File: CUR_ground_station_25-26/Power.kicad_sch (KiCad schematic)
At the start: 27 parts, among them J1 Conn_01x02, J2 UJ20-C-H-G-SMT-P16-TR, Q2 NTR4003N, SW5 PTS815SJM250SMTRLFS, U2 BQ24232RGT, U3 NCP186AMX330TAG, U4 USBLC6-2SC6

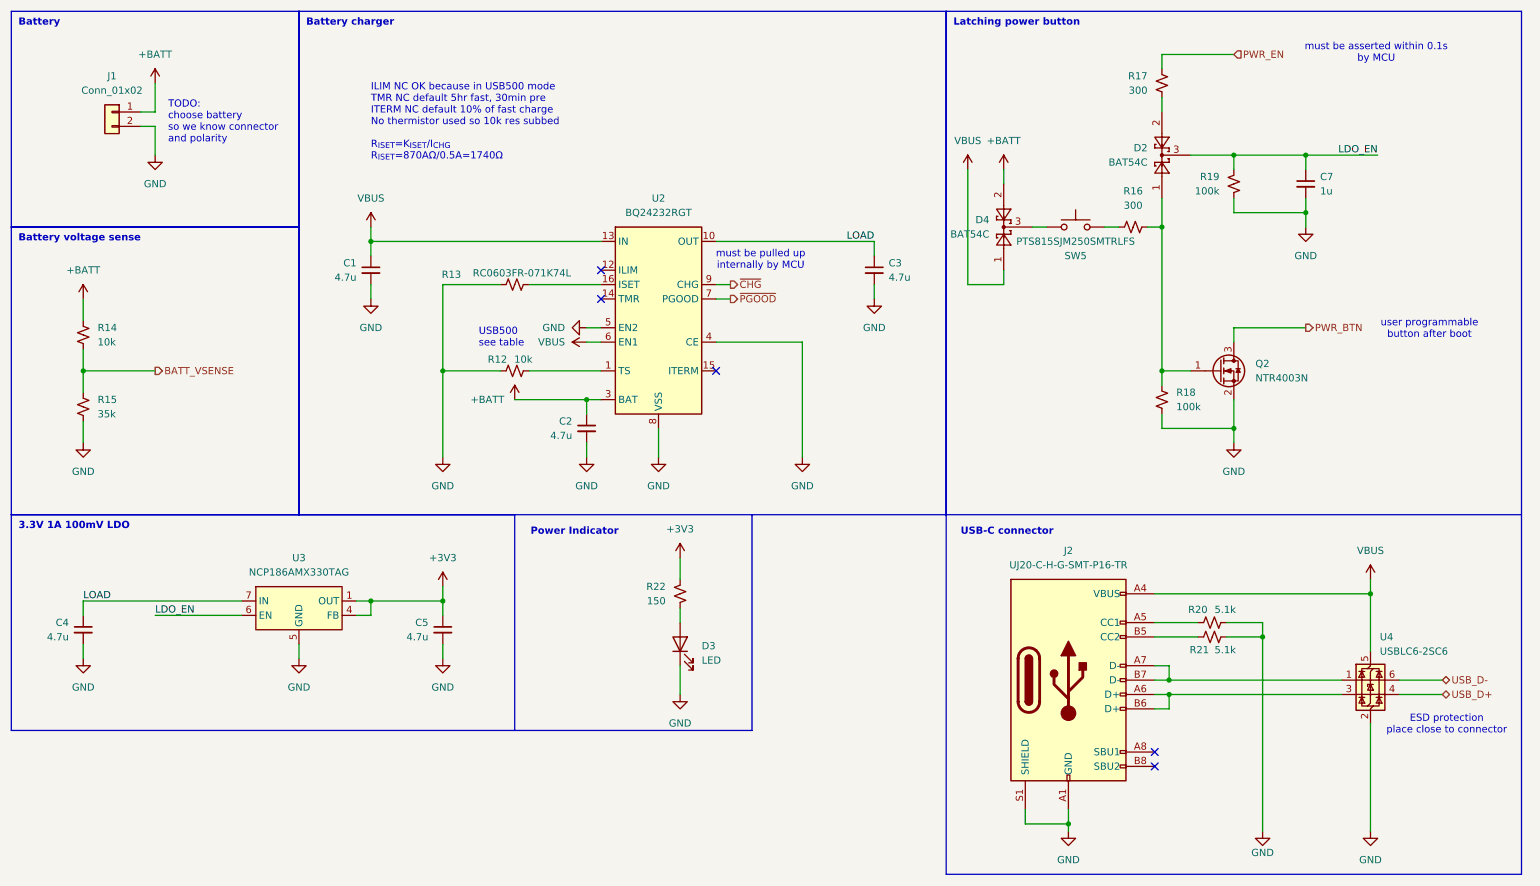
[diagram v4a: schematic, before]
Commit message: Add testpoints to power
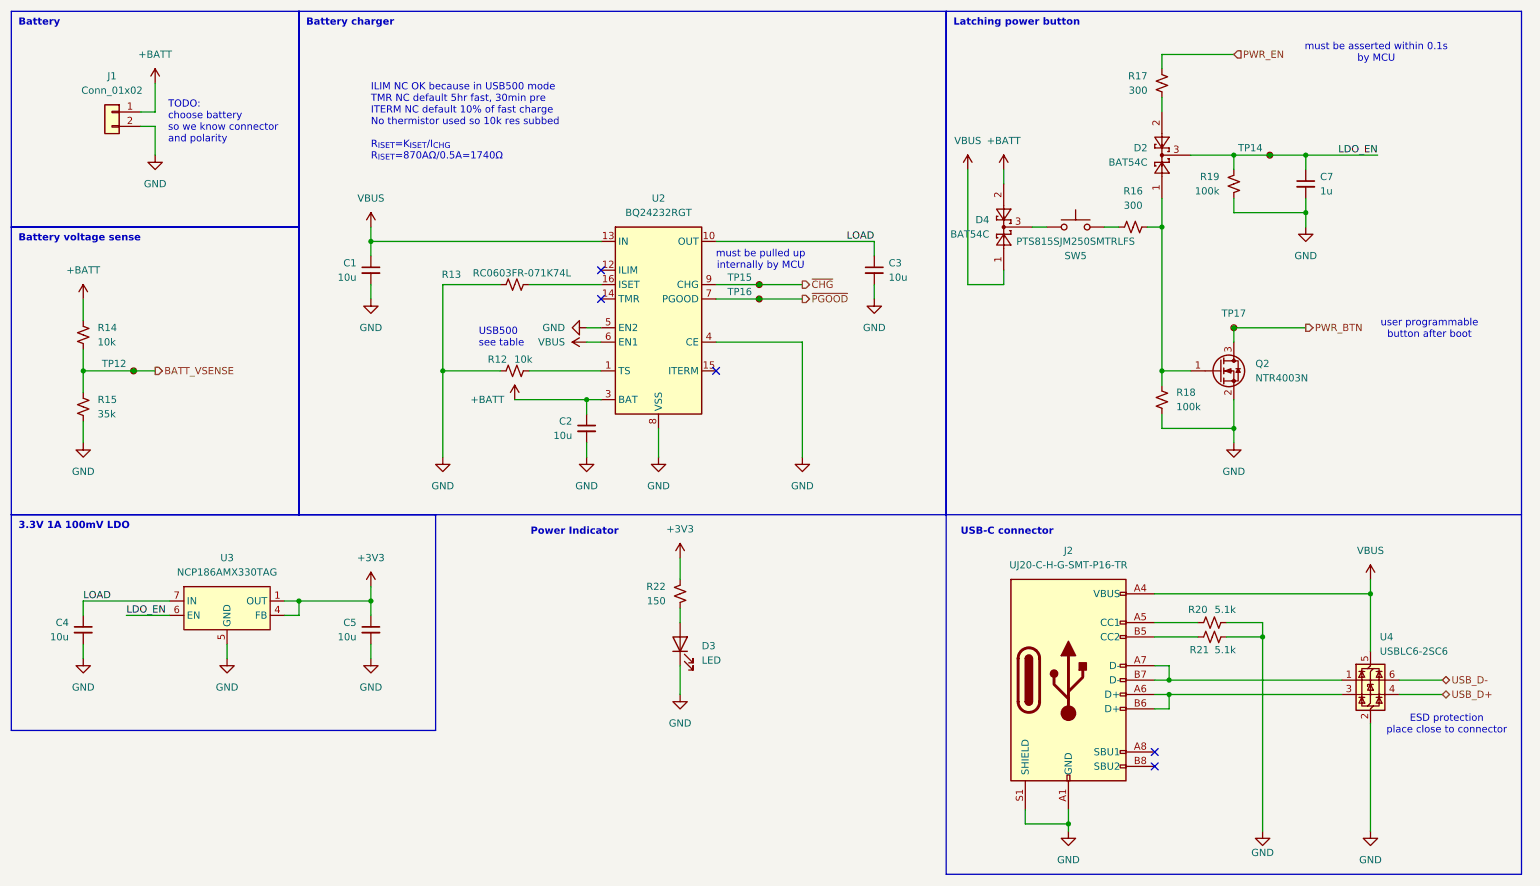
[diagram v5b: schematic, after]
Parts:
- added TP12, TP14, TP15, TP16, TP17: TestPoint_Small, TestPoint_KOASpeer:TestPoint_Chip_RCUCTE_0603, symbol Connector:TestPoint_Small
- C1, C2, C3, C4, C5: value 4.7u -> 10u
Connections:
- net BATT_VSENSE: now also TP12.1
- net LDO_EN: now also TP14.1
- net PWR_BTN: now also TP17.1
- net ~{CHG}: now also TP15.1
- net ~{PGOOD}: now also TP16.1
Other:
- moved on the sheet: C5, U3

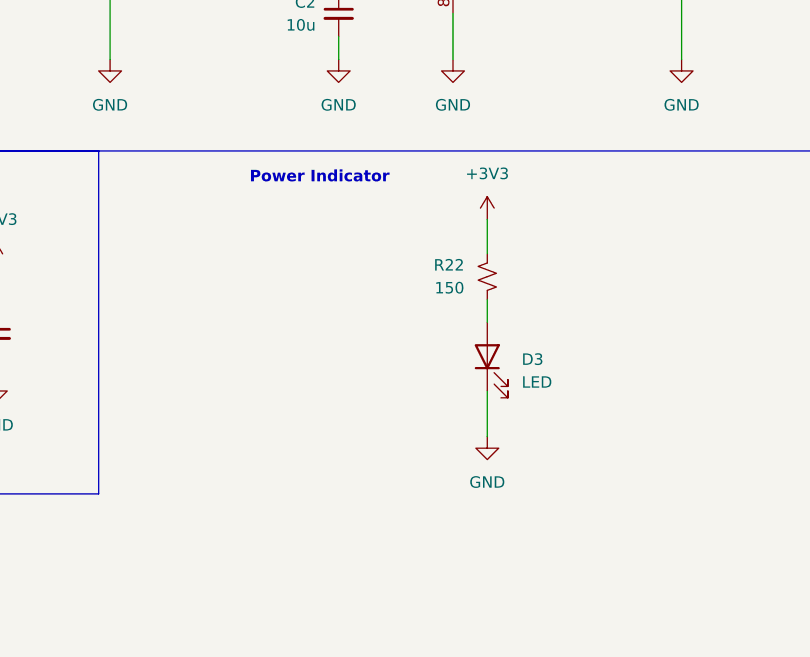
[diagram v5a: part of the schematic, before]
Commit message: Started placing pins on MCU
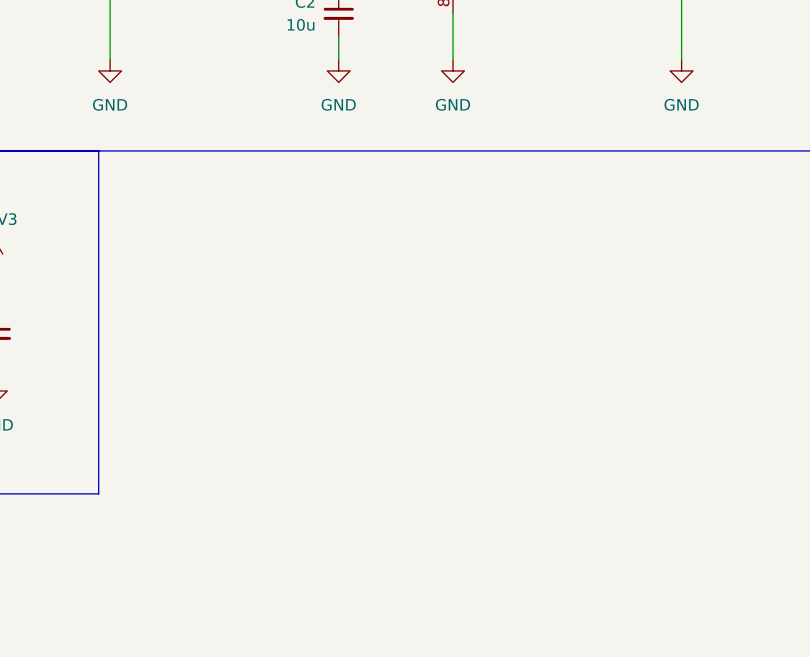
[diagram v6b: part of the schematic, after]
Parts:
- removed D3: LED, LED_SMD:LED_0603_1608Metric, symbol Device:LED
- removed R22: 150, Resistor_SMD:R_0603_1608Metric, symbol Device:R_Small_US
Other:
- note removed: "Power Indicator"

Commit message: updating footprints
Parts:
- C1, C2, C3, C4, C5: footprint (none) -> Capacitor_SMD:C_0603_1608Metric
- R12, R13, R14, R15: footprint (none) -> Resistor_SMD:R_0603_1608Metric
- R16, R17, R18, R19: footprint Resistor_SMD:R_0402_1005Metric -> Resistor_SMD:R_0603_1608Metric
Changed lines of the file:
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@@
 			)
 		)
-		(property "Footprint" ""
+		(property "Footprint" "Capacitor_SMD:C_0603_1608Metric"
 			(at 76.2 121.92 0)
 			(effects
@@
 			)
 		)
-		(property "Footprint" ""
+		(property "Footprint" "Resistor_SMD:R_0603_1608Metric"
 			(at 101.6 76.2 0)
 			(effects
@@
 			)
 		)
-		(property "Footprint" ""
+		(property "Footprint" "Resistor_SMD:R_0603_1608Metric"
 			(at 25.4 69.85 0)
 			(effects
@@
 			)
 		)
-		(property "Footprint" ""
+		(property "Footprint" "Capacitor_SMD:C_0603_1608Metric"
 			(at 165.1 58.42 0)
 			(effects
@@
 			)
 		)
-		(property "Footprint" "Resistor_SMD:R_0402_1005Metric"
+		(property "Footprint" "Resistor_SMD:R_0603_1608Metric"
 			(at 228.6 43.18 0)
 			(effects
@@
 			)
 		)
-		(property "Footprint" ""
+		(property "Footprint" "Capacitor_SMD:C_0603_1608Metric"
 			(at 76.2 58.42 0)
 			(effects
@@
 			)
 		)
-		(property "Footprint" ""
+		(property "Footprint" "Resistor_SMD:R_0603_1608Metric"
 			(at 101.6 60.96 0)
 			(effects
@@
 			)
 		)
-		(property "Footprint" "Resistor_SMD:R_0402_1005Metric"
+		(property "Footprint" "Resistor_SMD:R_0603_1608Metric"
 			(at 215.9 25.4 0)
 			(effects
@@
 			)
 		)
-		(property "Footprint" ""
+		(property "Footprint" "Resistor_SMD:R_0603_1608Metric"
 			(at 25.4 82.55 0)
 			(effects
@@
 			)
 		)
-		(property "Footprint" ""
+		(property "Footprint" "Capacitor_SMD:C_0603_1608Metric"
 			(at 25.4 121.92 0)
 			(effects
@@
 			)
 		)
-		(property "Footprint" ""
+		(property "Footprint" "Capacitor_SMD:C_0603_1608Metric"
 			(at 114.3 86.36 0)
 			(effects
@@
 			)
 		)
-		(property "Footprint" "Resistor_SMD:R_0402_1005Metric"
+		(property "Footprint" "Resistor_SMD:R_0603_1608Metric"
 			(at 210.82 50.8 0)
 			(effects
@@
 			)
 		)
-		(property "Footprint" "Resistor_SMD:R_0402_1005Metric"
+		(property "Footprint" "Resistor_SMD:R_0603_1608Metric"
 			(at 215.9 81.28 0)
 			(effects

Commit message: started layout-ing
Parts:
- J1: footprint (none) -> Connector_JST:JST_PH_B2B-PH-K_1x02_P2.00mm_Vertical
- U3: footprint Package_DFN_QFN:DFN-6-1EP_1.2x1.2mm_P0.4mm_EP0.3x0.94mm_PullBack -> XDFN8_1P6X1P2_onsemi:XDFN8_1P6X1P2_onsemi
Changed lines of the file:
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@@
 			)
 		)
-		(property "Footprint" "Package_DFN_QFN:DFN-6-1EP_1.2x1.2mm_P0.4mm_EP0.3x0.94mm_PullBack"
+		(property "Footprint" "XDFN8_1P6X1P2_onsemi:XDFN8_1P6X1P2_onsemi"
 			(at 50.8 114.3 0)
 			(effects
@@
 			)
 		)
-		(property "Footprint" ""
+		(property "Footprint" "Connector_JST:JST_PH_B2B-PH-K_1x02_P2.00mm_Vertical"
 			(at 30.48 30.48 0)
 			(effects
